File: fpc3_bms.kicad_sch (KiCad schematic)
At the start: 1 part

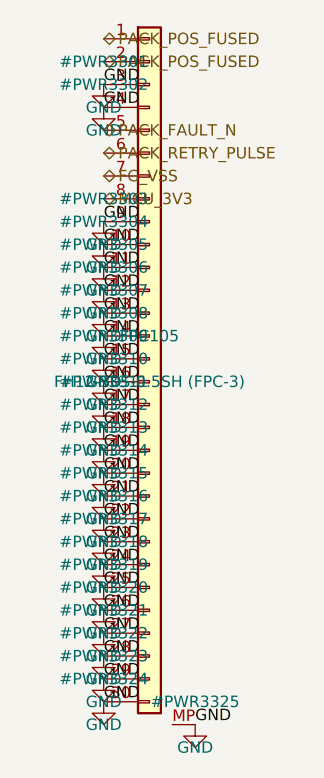
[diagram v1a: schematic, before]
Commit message: Phase 5: second-opinion audit remediation + rebuilt, verified board pipeline
Second-opinion AI audit found A-tier defects; remediation applied and the
board pipeline rebuilt on a known-good base with the fixes it needed:

- electrical: LTC4418IUF symbol pinout corrected (both selectors were
  dead as drawn); center charge cascade (U15 <- U15B, PD1 > PD2 > AUX);
  pack negative never crosses FPC-3, 15-pin FG_VSS return; power-budgeted
  FPC pin maps (0.4 A/pin derate); J12/DS4 completed; AUX source fuse
- FH41-68S footprint: 13 datasheet-correct SH pads + SH pin in symbol
- connector geometry settled against the Hirose FH12 2D drawing: FFC
  enters opposite the solder pins (mouth = local +Y); reversed side-B
  maps are correct for the 180-deg-mounted pairs; rotations set so mouths
  face across every seam
- pipeline (generate_split_boards.py): per-pin pad-net resync from the
  netlists (kills shadow nets for good), netlist-exact name
  normalization, netlist-only part injection (cascade, probe headers),
  zone refill after outline swap, read-before-write race fixed, orphan
  parts dropped loudly, non-zero exit on unresolved overlaps
- monolith board relocated to old/monolith_ducktop2.kicad_pcb (placement
  oracle for the center cut only)

verified end state: 4 boards 0 shorts / 0 clearance / 0 drill, 0 boundary
crossings, 6/6 connectors contract-exact with mouths facing, 0 shadow
nets, gates PASS x4, ERC 0 x4. routing next (499 nets/board).
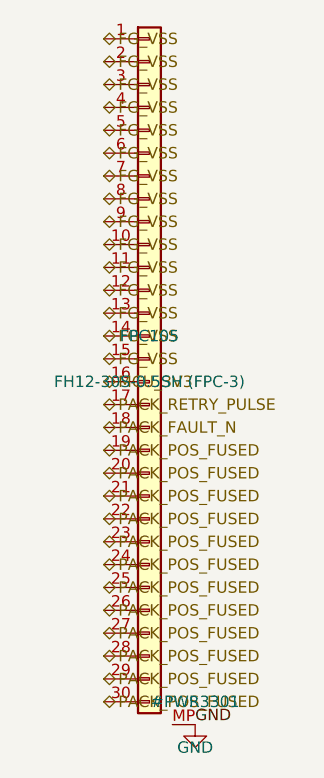
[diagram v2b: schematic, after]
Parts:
- FPC105: MPN (none) -> FH12-30S-0.5SH(55); Manufacturer (none) -> Hirose
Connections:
- net FG_VSS: now also FPC105.1 (Pin_1), FPC105.10 (Pin_10), FPC105.11 (Pin_11), FPC105.12 (Pin_12), FPC105.13 (Pin_13), FPC105.14 (Pin_14), FPC105.15 (Pin_15), FPC105.2 (Pin_2), FPC105.3 (Pin_3), FPC105.4 (Pin_4), FPC105.5 (Pin_5), FPC105.6 (Pin_6), FPC105.8 (Pin_8), FPC105.9 (Pin_9)
- net GND: no longer FPC105.10 (Pin_10), FPC105.11 (Pin_11), FPC105.12 (Pin_12), FPC105.13 (Pin_13), FPC105.14 (Pin_14), FPC105.15 (Pin_15), FPC105.16 (Pin_16), FPC105.17 (Pin_17), FPC105.18 (Pin_18), FPC105.19 (Pin_19), FPC105.20 (Pin_20), FPC105.21 (Pin_21), FPC105.22 (Pin_22), FPC105.23 (Pin_23), FPC105.24 (Pin_24), FPC105.25 (Pin_25), FPC105.26 (Pin_26), FPC105.27 (Pin_27), FPC105.28 (Pin_28), FPC105.29 (Pin_29), FPC105.3 (Pin_3), FPC105.30 (Pin_30), FPC105.4 (Pin_4), FPC105.9 (Pin_9)
- net MCU_3V3: now also FPC105.16 (Pin_16); no longer FPC105.8 (Pin_8)
- net PACK_FAULT_N: now also FPC105.18 (Pin_18); no longer FPC105.5 (Pin_5)
- net PACK_POS_FUSED: now also FPC105.19 (Pin_19), FPC105.20 (Pin_20), FPC105.21 (Pin_21), FPC105.22 (Pin_22), FPC105.23 (Pin_23), FPC105.24 (Pin_24), FPC105.25 (Pin_25), FPC105.26 (Pin_26), FPC105.27 (Pin_27), FPC105.28 (Pin_28), FPC105.29 (Pin_29), FPC105.30 (Pin_30); no longer FPC105.1 (Pin_1), FPC105.2 (Pin_2)
- net PACK_RETRY_PULSE: now also FPC105.17 (Pin_17); no longer FPC105.6 (Pin_6)

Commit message: fix audit issues and move some connectors
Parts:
- removed FPC105: FH12-30S-0.5SH (FPC-3), Connector_FFC-FPC:Hirose_FH12-30S-0.5SH_1x30-1MP_P0.50mm_Horizontal, symbol Conn_01x30_FFC_MP:Conn_01x30_FFC_MP
- added J2071: protected pack power, Connector_Molex:Molex_Micro-Fit_3.0_43650-0224_1x02-1MP_P3.00mm_Vertical, symbol Conn_01x02_MP:Conn_01x02_MP
- added J2073: isolated bms control, Connector_JST:JST_SH_SM05B-SRSS-TB_1x05-1MP_P1.00mm_Horizontal, symbol Connector_Generic_MountingPin:Conn_01x05_MountingPin
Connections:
- net FG_VSS: now also J2071.2 (Pin_2)
- net GND: now also J2073.5 (Pin_5), J2073.MP (MountPin)
- net MCU_3V3: now also J2073.3 (Pin_3)
- net PACK_FAULT_N: now also J2073.1 (Pin_1)
- net PACK_POS_FUSED: now also J2071.1 (Pin_1)
- net PACK_RETRY_PULSE: now also J2073.2 (Pin_2)
- new net PACK_CHG_TEMP_OK: J2073.4 (Pin_4)
- no-connect marks 0 -> 1
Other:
- note added: "j2071 carries pack current through the rated power harness. j2073 supplies the isolated control island and its own return."
- note added: "the bms control return never joins raw pack negative or the protected power return. the power return still crosses the center gauge shunt."

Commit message: fix the center layout and more board issues
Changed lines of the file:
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@@
   (on_board yes)
   (dnp no)
-  (property "Reference" "#PWR001" (at 74.93 92.71 0) (effects (font (size 1.27 1.27))))
+  (property "Reference" "#PWR3301" (at 74.93 92.71 0) (effects (font (size 1.27 1.27))))
   (property "Value" "GND" (at 74.93 97.79 0) (effects (font (size 1.27 1.27))))
   (property "Footprint" "" (at 74.93 95.25 0) (effects (font (size 1.27 1.27)) (hide yes)))
@@
     (project "ducktop2"
       (path "/46b21d0a-abb0-598b-9ae3-ea30d11d7d3c"
-        (reference "#PWR001")
+        (reference "#PWR3301")
         (unit 1)
       )
@@
   (on_board yes)
   (dnp no)
-  (property "Reference" "#PWR002" (at 80.01 97.79 0) (effects (font (size 1.27 1.27))))
+  (property "Reference" "#PWR3302" (at 80.01 97.79 0) (effects (font (size 1.27 1.27))))
   (property "Value" "GND" (at 80.01 102.87 0) (effects (font (size 1.27 1.27))))
   (property "Footprint" "" (at 80.01 100.33 0) (effects (font (size 1.27 1.27)) (hide yes)))
@@
     (project "ducktop2"
       (path "/46b21d0a-abb0-598b-9ae3-ea30d11d7d3c"
-        (reference "#PWR002")
+        (reference "#PWR3302")
         (unit 1)
       )
